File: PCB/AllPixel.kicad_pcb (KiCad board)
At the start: 2 copper layers, 68.5 x 24.5 mm, 28 parts, among them CON1 ML_USB_MINI, CON2 BARREL_JACK, Q1 NPN, U1 ATMEGA16U4/32U4, Y1 16MHz

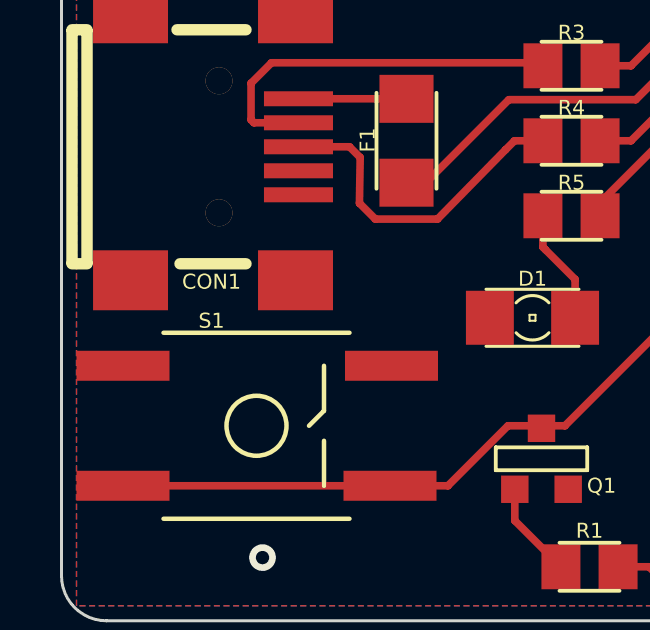
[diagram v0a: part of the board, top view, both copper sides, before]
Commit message: Modified USB footprint to center anchor.
AP: Modified USB footprint to center anchor.
AP: Generated position file for SMD components
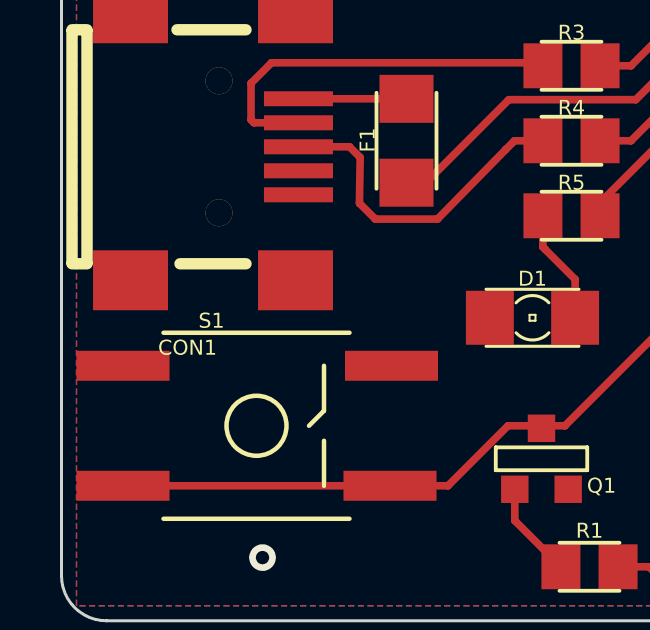
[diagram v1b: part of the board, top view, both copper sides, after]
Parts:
- moved CON1 2.34 mm to (18.4, 27.2)
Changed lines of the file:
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@@
 (kicad_pcb (version 3) (host pcbnew "(2013-07-07 BZR 4022)-stable")
   (general
-    (links 65)
+    (links 0)
     (no_connects 5)
-    (area 12.685512 12.650002 94.499998 43.829)
+    (area 13.949999 18.449999 82.550001 43.050001)
     (thickness 1.6)
     (drawings 12)
@@
   (page A3)
   (layers
-    (15 F.Cu signal hide)
+    (15 F.Cu signal)
     (0 B.Cu signal hide)
     (16 B.Adhes user)
@@
     (pad_drill 1)
     (pad_to_mask_clearance 0)
-    (aux_axis_origin 0 0)
-    (visible_elements 7FFFFB3F)
+    (aux_axis_origin 14 18.5)
+    (visible_elements 7FFFFBBF)
     (pcbplotparams
       (layerselection 283148289)
@@
     (descr "SMALL SOLDER JUMPER WITH NO PASTE LAYER SO IT WILL OPEN AFTER REFLOW.")
     (tags "SMALL SOLDER JUMPER WITH NO PASTE LAYER SO IT WILL OPEN AFTER REFLOW.")
-    (attr smd)
     (fp_text reference SJ2 (at 0.10668 -1.4732 45) (layer B.SilkS) hide
       (effects (font (size 0.4064 0.4064) (thickness 0.0889)))
@@
     (descr "SMALL SOLDER JUMPER WITH NO PASTE LAYER SO IT WILL OPEN AFTER REFLOW.")
     (tags "SMALL SOLDER JUMPER WITH NO PASTE LAYER SO IT WILL OPEN AFTER REFLOW.")
-    (attr smd)
     (fp_text reference SJ3 (at 0.10668 -1.4732 315) (layer B.SilkS) hide
       (effects (font (size 0.4064 0.4064) (thickness 0.0889)))
@@
   (module ML_Tactile-SMT (layer F.Cu)
     (at 20.5 36.5)
+    (attr smd)
     (fp_text reference S1 (at -1.5 -3.5) (layer F.SilkS)
       (effects (font (size 0.5 0.5) (thickness 0.06096)))
@@
     (at 25.5 27 90)
     (descr "SMT capacitor, 1206")
+    (attr smd)
     (fp_text reference F1 (at 0.0254 -1.2954 90) (layer F.SilkS)
       (effects (font (size 0.5 0.5) (thickness 0.06096)))
@@
     (at 31 24.5)
     (descr "SMT capacitor, 0805")
+    (attr smd)
     (fp_text reference R3 (at 0 -1.1) (layer F.SilkS)
       (effects (font (size 0.5 0.5) (thickness 0.06096)))
@@
     (at 31 27)
     (descr "SMT capacitor, 0805")
+    (attr smd)
     (fp_text reference R4 (at 0 -1.1) (layer F.SilkS)
       (effects (font (size 0.5 0.5) (thickness 0.06096)))
@@
     (at 31 29.5)
     (descr "SMT capacitor, 0805")
+    (attr smd)
     (fp_text reference R5 (at 0 -1.1) (layer F.SilkS)
       (effects (font (size 0.5 0.5) (thickness 0.06096)))
@@
     (at 42.1 25.6)
     (descr "SMT capacitor, 0805")
+    (attr smd)
     (fp_text reference R2 (at 0 -1.1) (layer F.SilkS)
       (effects (font (size 0.5 0.5) (thickness 0.06096)))
@@
     (at 42.1 28.1)
     (descr "SMT capacitor, 0805")
+    (attr smd)
     (fp_text reference R8 (at 0 -1.1) (layer F.SilkS)
       (effects (font (size 0.5 0.5) (thickness 0.06096)))
@@
     (at 58.5 32.8 90)
     (descr "SMT capacitor, 1206")
+    (attr smd)
     (fp_text reference C4 (at 2.8 0 180) (layer F.SilkS)
       (effects (font (size 0.5 0.5) (thickness 0.06096)))
@@
     (at 58.5 38.8 270)
     (descr "SMT capacitor, 1206")
+    (attr smd)
     (fp_text reference C3 (at 2.9 0 360) (layer F.SilkS)
       (effects (font (size 0.5 0.5) (thickness 0.06096)))
@@
     (at 31.6 41.2 180)
     (descr "SMT capacitor, 0805")
+    (attr smd)
     (fp_text reference R1 (at 0 1.2 180) (layer F.SilkS)
       (effects (font (size 0.5 0.5) (thickness 0.06096)))
@@
       (layers *.Cu *.Mask F.SilkS)
       (net 4 GND)
-    )
-  )
-  (module ML_USB_MINI_posts (layer F.Cu)
-    (at 19.25 25)
-    (descr "USB Mini-B 5-pin SMD connector")
-    (tags "USB, Mini-B, connector")
-    (fp_text reference CON1 (at -0.25 6.7) (layer F.SilkS)
-      (effects (font (size 0.5 0.5) (thickness 0.06096)))
-    )
-    (fp_text value ML_USB_MINI (at 0 -7.0993) (layer F.SilkS) hide
-      (effects (font (size 1.016 1.016) (thickness 0.2032)))
-    )
-    (fp_line (start -4.9 6.1) (end -4.4 6.1) (layer F.SilkS) (width 0.381))
-    (fp_line (start -4.9 -1.7) (end -4.4 -1.7) (layer F.SilkS) (width 0.381))
-    (fp_line (start -1.4 -1.7) (end 0.9 -1.7) (layer F.SilkS) (width 0.381))
-    (fp_line (start -1.3 6.1) (end 0.9 6.1) (layer F.SilkS) (width 0.381))
-    (fp_line (start -4.39918 -1.65064) (end -4.39918 6.05064) (layer F.SilkS) (width 0.381))
-    (fp_line (start -4.89994 -1.65064) (end -4.89994 6.05064) (layer F.SilkS) (width 0.381))
-    (pad 1 smd rect (at 2.64932 0.5998) (size 2.30124 0.50038)
-      (layers F.Cu F.Paste F.Mask)
-      (net 1 +5V)
-    )
-    (pad 2 smd rect (at 2.64932 1.3999) (size 2.30124 0.50038)
-      (layers F.Cu F.Paste F.Mask)
-      (net 7 N-0000012)
-    )
-    (pad 3 smd rect (at 2.64932 2.2) (size 2.30124 0.50038)
-      (layers F.Cu F.Paste F.Mask)
-      (net 8 N-0000013)
-    )
-    (pad 4 smd rect (at 2.64932 3.0001) (size 2.30124 0.50038)
-      (layers F.Cu F.Paste F.Mask)
-    )
-    (pad 5 smd rect (at 2.64932 3.8002) (size 2.30124 0.50038)
-      (layers F.Cu F.Paste F.Mask)
-      (net 4 GND)
-    )
-    (pad 6 smd rect (at 2.55026 -2.25008) (size 2.49936 1.99898)
-      (layers F.Cu F.Paste F.Mask)
-    )
-    (pad 7 smd rect (at -2.94884 -2.25008) (size 2.49936 1.99898)
-      (layers F.Cu F.Paste F.Mask)
-    )
-    (pad 8 smd rect (at 2.55026 6.65008) (size 2.49936 1.99898)
-      (layers F.Cu F.Paste F.Mask)
-    )
-    (pad 9 smd rect (at -2.94884 6.65008) (size 2.49936 1.99898)
-      (layers F.Cu F.Paste F.Mask)
-    )
-    (pad h1 thru_hole circle (at 0 0) (size 0.9 0.9) (drill 0.9)
-      (layers *.Cu F.Paste F.SilkS F.Mask)
-    )
-    (pad h2 thru_hole circle (at 0 4.4) (size 0.9 0.9) (drill 0.9)
-      (layers *.Cu F.Paste F.SilkS F.Mask)
     )
   )
@@
       (layers F.Cu F.Paste F.Mask)
       (net 4 GND)
+    )
+  )
+  (module ML_USB_MINI_posts (layer F.Cu)
+    (at 18.45 27.2)
+    (descr "USB Mini-B 5-pin SMD connector")
+    (tags "USB, Mini-B, connector")
+    (attr smd)
+    (fp_text reference CON1 (at -0.25 6.7) (layer F.SilkS)
+      (effects (font (size 0.5 0.5) (thickness 0.06096)))
+    )
+    (fp_text value ML_USB_MINI (at 0 -7.0993) (layer F.SilkS) hide
+      (effects (font (size 1.016 1.016) (thickness 0.2032)))
+    )
+    (fp_line (start -4.1 3.9) (end -3.6 3.9) (layer F.SilkS) (width 0.381))
+    (fp_line (start -4.1 -3.9) (end -3.6 -3.9) (layer F.SilkS) (width 0.381))
+    (fp_line (start -0.6 -3.9) (end 1.7 -3.9) (layer F.SilkS) (width 0.381))
+    (fp_line (start -0.5 3.9) (end 1.7 3.9) (layer F.SilkS) (width 0.381))
+    (fp_line (start -3.59918 -3.85064) (end -3.59918 3.85064) (layer F.SilkS) (width 0.381))
+    (fp_line (start -4.09994 -3.85064) (end -4.09994 3.85064) (layer F.SilkS) (width 0.381))
+    (pad 1 smd rect (at 3.44932 -1.6002) (size 2.30124 0.50038)
+      (layers F.Cu F.Paste F.Mask)
+      (net 1 +5V)
+    )
+    (pad 2 smd rect (at 3.44932 -0.8001) (size 2.30124 0.50038)
+      (layers F.Cu F.Paste F.Mask)
+      (net 7 N-0000012)
+    )
+    (pad 3 smd rect (at 3.44932 0) (size 2.30124 0.50038)
+      (layers F.Cu F.Paste F.Mask)
+      (net 8 N-0000013)
+    )
+    (pad 4 smd rect (at 3.44932 0.8001) (size 2.30124 0.50038)
+      (layers F.Cu F.Paste F.Mask)
+    )
+    (pad 5 smd rect (at 3.44932 1.6002) (size 2.30124 0.50038)
+      (layers F.Cu F.Paste F.Mask)
+      (net 4 GND)
+    )
+    (pad 6 smd rect (at 3.35026 -4.45008) (size 2.49936 1.99898)
+      (layers F.Cu F.Paste F.Mask)
+    )
+    (pad 7 smd rect (at -2.14884 -4.45008) (size 2.49936 1.99898)
+      (layers F.Cu F.Paste F.Mask)
+    )
+    (pad 8 smd rect (at 3.35026 4.45008) (size 2.49936 1.99898)
+      (layers F.Cu F.Paste F.Mask)
+    )
+    (pad 9 smd rect (at -2.14884 4.45008) (size 2.49936 1.99898)
+      (layers F.Cu F.Paste F.Mask)
+    )
+    (pad h1 thru_hole circle (at 0.8 -2.2) (size 0.9 0.9) (drill 0.9)
+      (layers *.Cu F.Paste F.SilkS F.Mask)
+    )
+    (pad h2 thru_hole circle (at 0.8 2.2) (size 0.9 0.9) (drill 0.9)
+      (layers *.Cu F.Paste F.SilkS F.Mask)
     )
   )
@@
   (segment (start 60.9737 33.1263) (end 62.5719 34.7245) (width 0.254) (layer B.Cu) (net 6))
   (segment (start 21.89932 26.3999) (end 20.4174 26.3999) (width 0.254) (layer F.Cu) (net 7))
-  (segment (start 29.7785 24.4785) (end 30.0475 24.5) (width 0.254) (layer F.Cu) (net 7))
   (segment (start 20.3174 26.2999) (end 20.3174 25.0823) (width 0.254) (layer F.Cu) (net 7))
   (segment (start 20.3174 25.0823) (end 21 24.4) (width 0.254) (layer F.Cu) (net 7))
+  (segment (start 20.4174 26.3999) (end 20.3174 26.2999) (width 0.254) (layer F.Cu) (net 7))
+  (segment (start 29.7785 24.4785) (end 30.0475 24.5) (width 0.254) (layer F.Cu) (net 7))
   (segment (start 21 24.4) (end 29.7 24.4) (width 0.254) (layer F.Cu) (net 7))
   (segment (start 29.7 24.4) (end 29.7785 24.4785) (width 0.254) (layer F.Cu) (net 7))
-  (segment (start 20.4174 26.3999) (end 20.3174 26.2999) (width 0.254) (layer F.Cu) (net 7))
   (segment (start 21.89932 27.2) (end 23.6 27.2) (width 0.254) (layer F.Cu) (net 8))
   (segment (start 29.1 27) (end 28.8 27.3) (width 0.254) (layer F.Cu) (net 8))

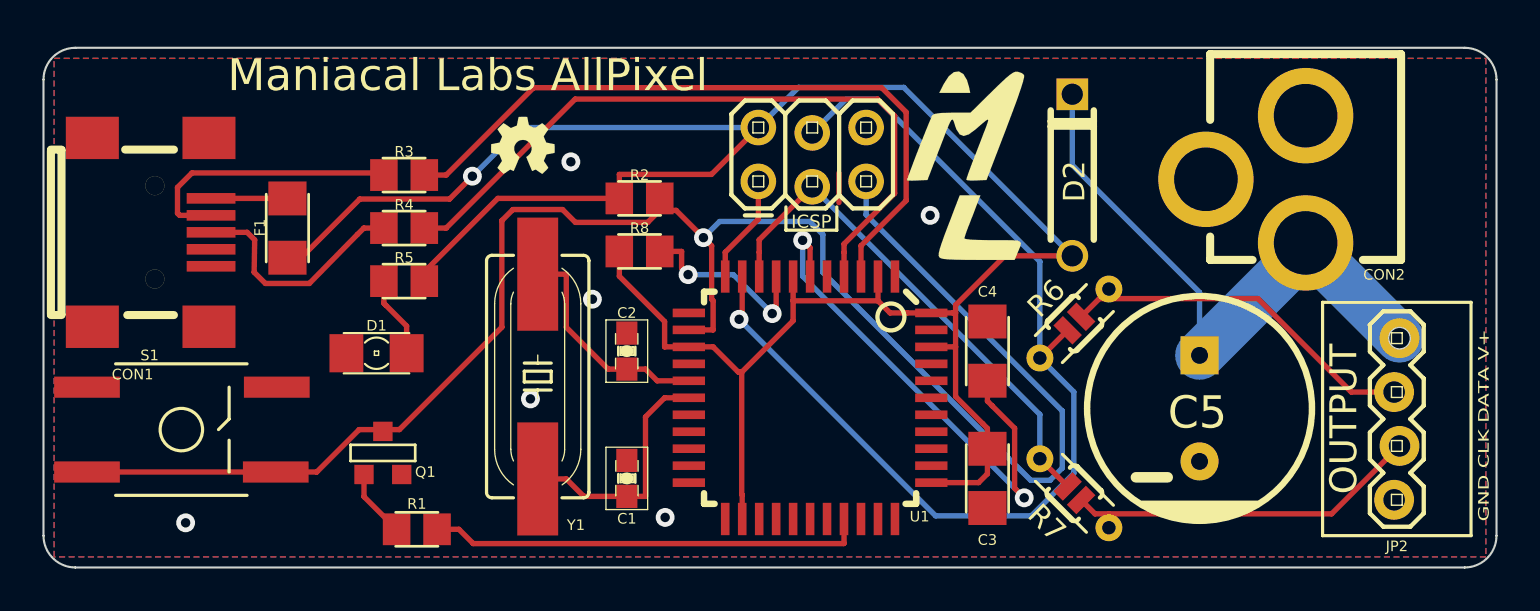
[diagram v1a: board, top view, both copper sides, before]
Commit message: Modified Jack and Switch Ftprnt, Fixed Via Issue
Changed barrel jack footprint (3.5mm holes), changed switch pad spacing
(5.5mm), fixed ground vias so that DRC passes with no unconnected pads
and ground fill works correctly. Also added small trace between ICSP GND
and ATMega pin 5 (think this was UGND?)
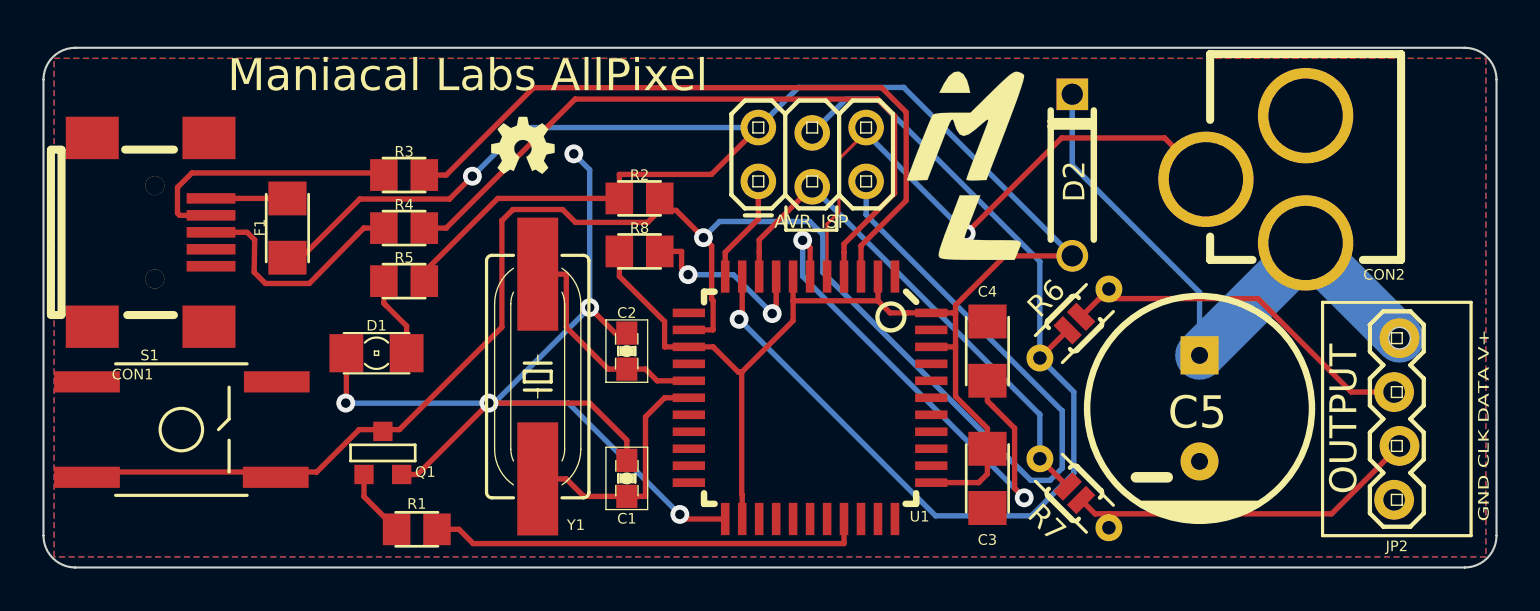
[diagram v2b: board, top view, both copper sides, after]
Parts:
- CON2: footprint ML_BARREL_JACK_ROUND_PADS_SHORT -> ML_BARREL_JACK_ROUND_PADS_SHORT_3_5mmHoles
- JP1: value ICSP -> AVR_ISP
- S1: footprint ML_Tactile-SMT -> ML_Tactile-SMT_5.5
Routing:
- net GND: track 0.00 -> 81.3 mm, vias 0 -> 6
- net (no net): track 1.40 -> 0.00 mm, vias 6 -> 0
